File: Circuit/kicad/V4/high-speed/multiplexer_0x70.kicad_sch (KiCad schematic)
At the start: 17 parts, among them U18 TCA9548APWR

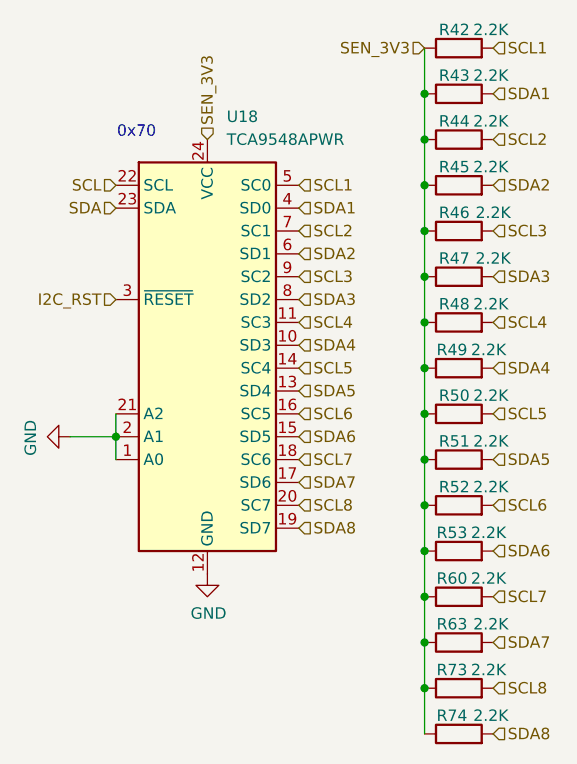
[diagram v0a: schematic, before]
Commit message: High Speed all routed, DRC, DFM shows 0 error (without silkscreen layers)
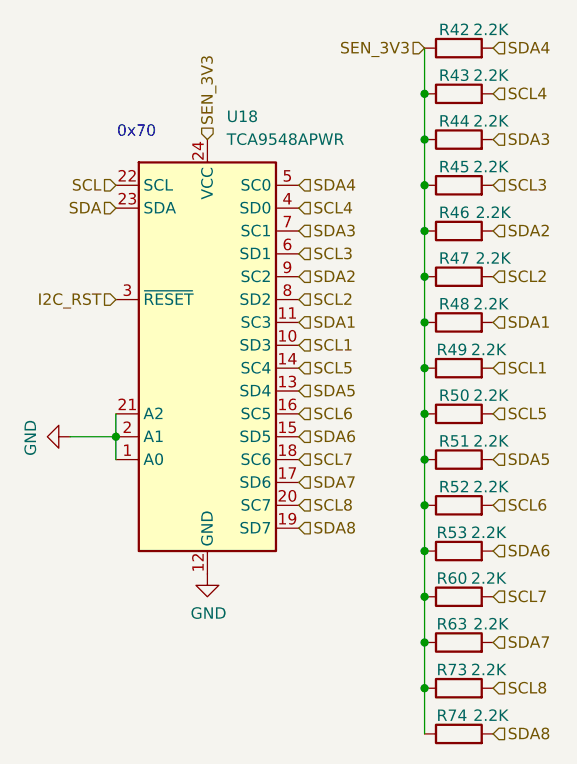
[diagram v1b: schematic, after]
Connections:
- net SCL1: now also R49.2, U18.10 (SD3); no longer R42.2, U18.5 (SC0)
- net SCL2: now also R47.2, U18.8 (SD2); no longer R44.2, U18.7 (SC1)
- net SCL3: now also R45.2, U18.6 (SD1); no longer R46.2, U18.9 (SC2)
- net SCL4: now also R43.2, U18.4 (SD0); no longer R48.2, U18.11 (SC3)
- net SDA1: now also R48.2, U18.11 (SC3); no longer R43.2, U18.4 (SD0)
- net SDA2: now also R46.2, U18.9 (SC2); no longer R45.2, U18.6 (SD1)
- net SDA3: now also R44.2, U18.7 (SC1); no longer R47.2, U18.8 (SD2)
- net SDA4: now also R42.2, U18.5 (SC0); no longer R49.2, U18.10 (SD3)
